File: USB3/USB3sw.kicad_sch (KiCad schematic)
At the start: 0 parts

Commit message: usb3 work cont
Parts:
- added C19: 1uF/10V, symbol Device:C_Polarized
- added C20, C21: 22uF/10V, symbol Device:C_Polarized
- added C22: 0.1uF/16V, symbol Device:C_Polarized
- added R20: 120K, symbol Device:R
- added R21: 6.8k/1%, symbol Device:R
- added U9: ~, symbol raxda:SGM2576YN5G/TR
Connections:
- new net: R21.1, U9.3 (OCB)
- new net Camera_GPIO: R20.1, U9.4 (EN)
- new net GND: C19.2, C20.2, C21.2, C22.2, R20.2, R21.2, U9.2 (GND)
- new net VCC5V0_USB: C19.1, U9.5 (IN)
- new net VCC5V0_USB3: C20.1, C21.1, C22.1, U9.1 (VOUT)

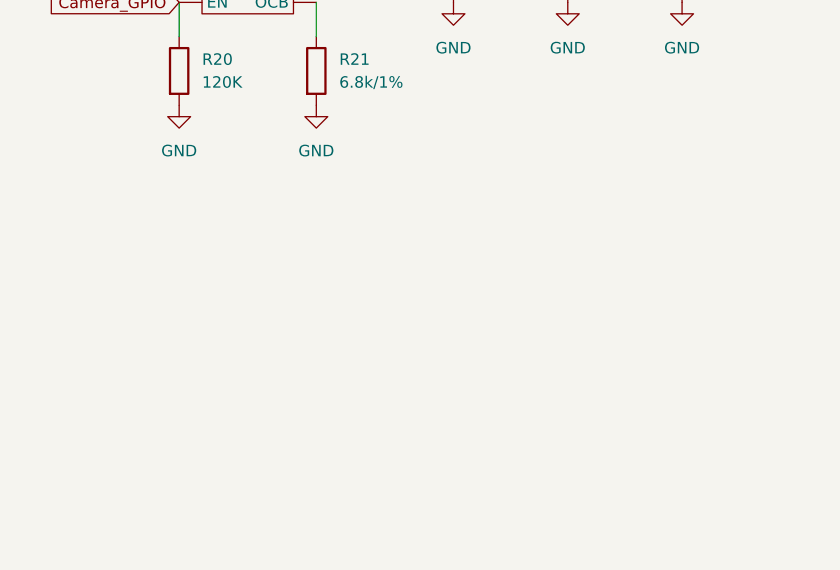
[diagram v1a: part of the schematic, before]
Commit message: usb3 down done
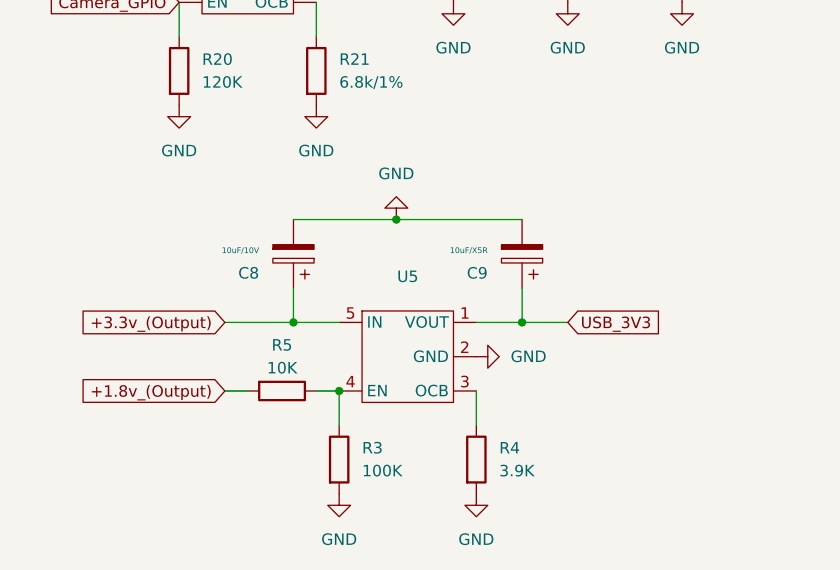
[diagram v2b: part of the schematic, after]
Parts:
- added C8: 10uF/10V, symbol Device:C_Polarized
- added C9: 10uF/X5R, symbol Device:C_Polarized
- added R3: 100K, symbol Device:R
- added R4: 3.9K, symbol Device:R
- added R5: 10K, symbol Device:R
- added U5: ~, symbol raxda:SGM2576YN5G/TR
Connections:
- net GND: now also C8.2, C9.2, R3.2, R4.2, U5.2 (GND)
- new net: R4.1, U5.3 (OCB)
- new net: R3.1, R5.1, U5.4 (EN)
- new net +1.8v_(Output): R5.2
- new net +3.3v_(Output): C8.1, U5.5 (IN)
- new net USB_3V3: C9.1, U5.1 (VOUT)

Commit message: finished usb3.0
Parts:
- removed C20, C21: 22uF/10V, symbol Device:C_Polarized
- removed C22: 0.1uF/16V, symbol Device:C_Polarized
- removed R20: 120K, symbol Device:R
- removed R21: 6.8k/1%, symbol Device:R
- removed U9: ~, symbol raxda:SGM2576YN5G/TR
- added C35, C36, C37, C39, C41, C43: 0.1uF, symbol Device:C
- added C38, C40, C42, C44: 150uF, symbol Device:C_Polarized
- added R12, R28: 25.5K 0402 5%, symbol Device:R
- added R13, R14, R15, R16: 10K 0402 5%, symbol Device:R
- added R24, R25, R26, R27: 4.7K 0402 5%, symbol Device:R
- added U3, U6: TPS2561, Package_SON:VSON-10-1EP_3x3mm_P0.5mm_EP1.65x2.4mm_ThermalVias, symbol Interface_USB:TPS2561
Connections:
- net +1.8v_(Output) is gone; now on net Camera_GPIO: R5.2
- net GND: now also C35.2, C36.1, C37.2, C38.2, C39.2, C40.2, C41.2, C42.2, C43.2, C44.2, R12.2, R24.1, R25.1, R26.1, R27.1, R28.1, U3.1 (GND), U3.11 (PAD), U6.1 (GND), U6.11 (PAD)
- net USB_3V3: now also R13.2, R14.2, R15.1, R16.1
- net VCC5V0_USB: now also C35.1, C36.2, U3.2 (IN), U3.3 (IN), U6.2 (IN), U6.3 (IN)
- new net: R12.1, U6.7 (ILM)
- new net: R28.2, U3.7 (ILM)
- new net DN1_VBUS: C41.1, C42.1, U3.9 (OUT1)
- new net DN2_VBUS: C43.1, C44.1, U3.8 (OUT2)
- new net DN3_VBUS: C37.1, C38.1, U6.9 (OUT1)
- new net DN4_VBUS: C39.1, C40.1, U6.8 (OUT2)
- new net OVERCUR1Z: R13.1, U3.10 (~{FAULT1})
- new net OVERCUR2Z: R14.1, U3.6 (~{FAULT2})
- new net OVERCUR3Z: R15.2, U6.10 (~{FAULT1})
- new net OVERCUR4Z: R16.2, U6.6 (~{FAULT2})
- new net PWRCTRL1_BATEN1: R25.2, U3.4 (EN1)
- new net PWRCTRL2_BATEN2: R24.2, U3.5 (EN2)
- new net PWRCTRL3_BATEN3: R26.2, U6.4 (EN1)
- new net PWRCTRL4_BATEN4: R27.2, U6.5 (EN2)

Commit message: usbc work
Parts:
- U5: value ~ -> SGM2576
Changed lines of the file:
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@@
 		(fields_autoplaced yes)
 		(property "Reference" "U5"
-			(at 55.88 69.85 0)
+			(at 55.88 68.58 0)
 			(effects
 				(font
@@
 			)
 		)
-		(property "Value" "~"
-			(at 55.88 72.39 0)
+		(property "Value" "SGM2576"
+			(at 55.88 71.12 0)
 			(effects
 				(font
